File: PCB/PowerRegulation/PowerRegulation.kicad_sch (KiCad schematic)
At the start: 130 parts, among them J1 USB_C_Receptacle_USB2.0_14P, J2 AudioJack3_Ground_Switch, J3 Wii audio in, J4 OLED, SW1 RESET, SW2 BOOT, U1 BQ25883RGER, U10 MCP4651-503E/ST, U11 PAM8403, U2 TPS22918DBVR, U3 STM32F072CBTx, U4 TPS22918DBVR, U5 TPS563200DDCR, U6 TPS563200DDCR, U7 TPS563200DDCR, U8 TPS563200DDCR, U9 TPS563200DDCR

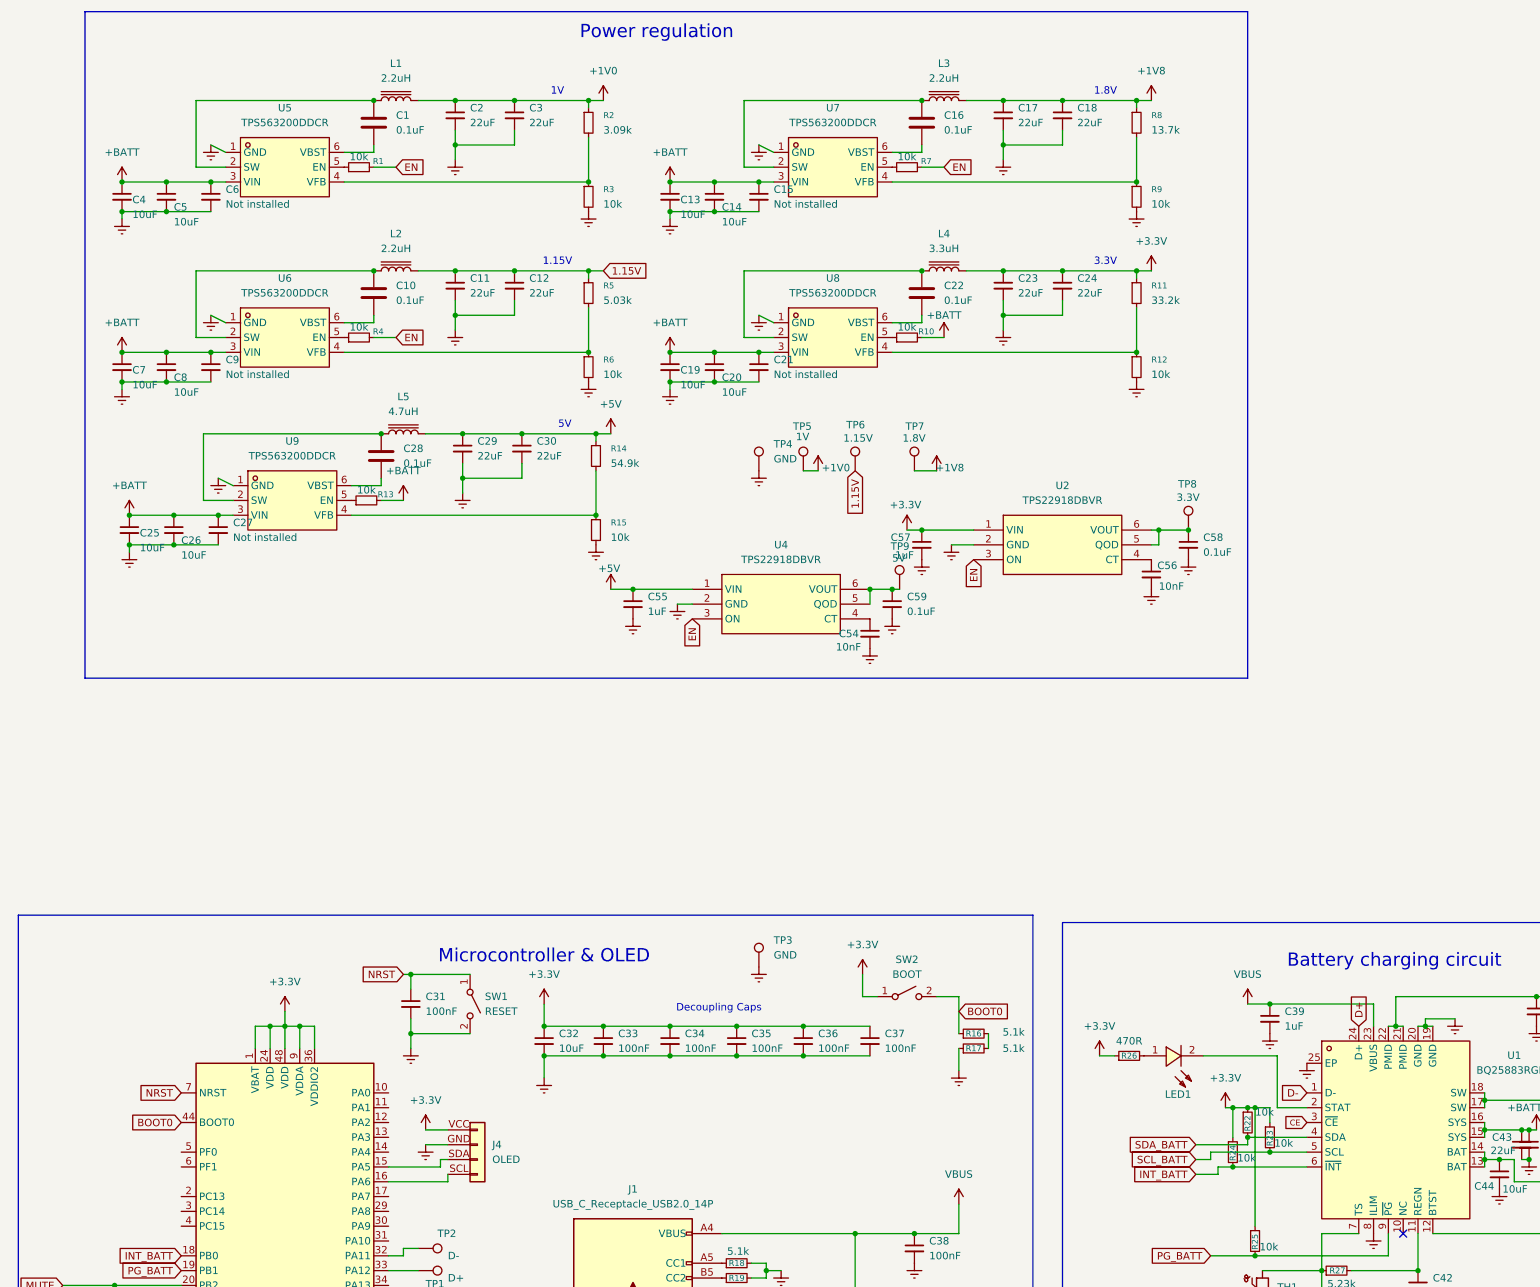
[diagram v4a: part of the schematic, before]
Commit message: Add grounded screws
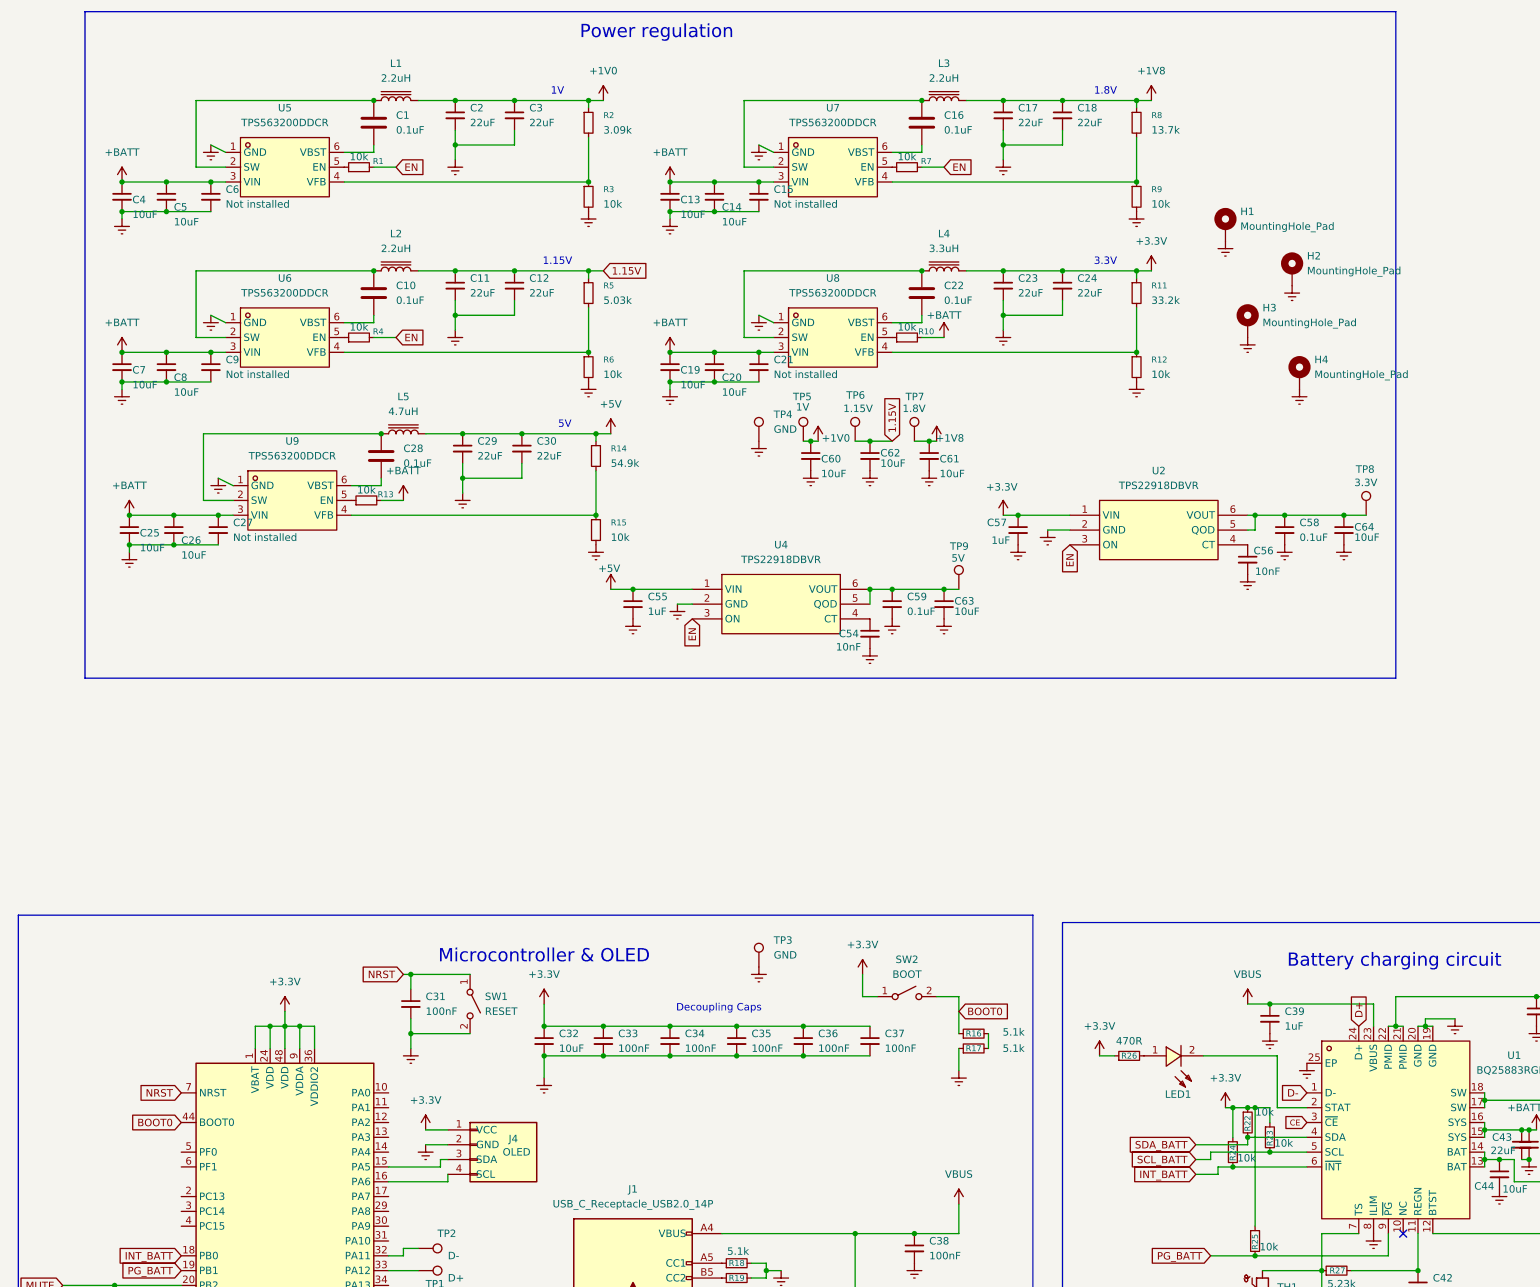
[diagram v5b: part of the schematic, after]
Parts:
- added C60, C61, C62, C63, C64: 10uF, EasyEDA:R0805, symbol Device:C_Small
- added H1, H2, H3, H4: MountingHole_Pad, MountingHole:MountingHole_3.2mm_M3_Pad_Via, symbol Mechanical:MountingHole_Pad
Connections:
- net +1V0: now also C60.1
- net +1V8: now also C61.1
- net +3.3V: now also J4.1 (VCC); no longer J4.VCC (Pin_1)
- net 1.15V: now also C62.1
- net GNDREF: now also J4.2 (GND), C60.2, C61.2, C62.2, C63.2, C64.2, H1.1, H2.1, H3.1, H4.1; no longer J4.GND (Pin_2)
- net at C58.1, TP8.1, U2.5 (QOD)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: now also C64.1
- net at U3.16 (PA6): now also J4.4 (SCL); no longer J4.SCL (Pin_4)
- net at U3.15 (PA5): now also J4.3 (SDA); no longer J4.SDA (Pin_3)
- net at C59.1, TP9.1, U4.5 (QOD)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: now also C63.1
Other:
- moved on the sheet: C56, C57, C58, TP4, TP5, TP6, TP7, TP8, TP9, U2

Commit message: make logo, route some stuff
THIS IS BEFORE THE BATT+ ON In2.Cu
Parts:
- removed J1: USB_C_Receptacle_USB2.0_14P, EasyEDA:USB-C-SMD_TYPE-C-16PIN-2MD-073, symbol Connector:USB_C_Receptacle_USB2.0_14P
- added J1: USB_C_Receptacle_USB2.0_16P, Connector_USB:USB_C_Receptacle_Palconn_UTC16-G, symbol Connector:USB_C_Receptacle_USB2.0_16P
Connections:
- net CE: now also U3.46 (PB9)
- net D+: now also J1.A6 (D+), J1.B6 (D+)
- net D-: now also J1.A7 (D-), J1.B7 (D-)
- net GNDREF: now also J1.A1 (GND), J1.A12 (GND), J1.B1 (GND), J1.B12 (GND), J1.SH (SHIELD)
- net VBUS: now also J1.A4 (VBUS), J1.A9 (VBUS), J1.B4 (VBUS), J1.B9 (VBUS)
- net Debug+: now reaches TP1.1, U3.33 (PA12)
- net at R18.1: now also J1.A5 (CC1)
- net Debug-: now reaches TP2.1, U3.32 (PA11)
- net at R19.1: now also J1.B5 (CC2)
- no-connect marks 3 -> 28
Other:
- moved on the sheet: TP1, TP2

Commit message: route the board
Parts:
- removed J2: AudioJack3_Ground_Switch, symbol Connector_Audio:AudioJack3_Ground_Switch
- added TP12, TP13: TestPoint, TestPoint:TestPoint_Pad_D1.0mm, symbol Connector:TestPoint
- added TP14: L+, TestPoint:TestPoint_Pad_D2.5mm, symbol Connector:TestPoint
- added TP15: R+, TestPoint:TestPoint_Pad_D2.5mm, symbol Connector:TestPoint
- added TP16: GND, TestPoint:TestPoint_Pad_D2.5mm, symbol Connector:TestPoint
- added TP17: L-, TestPoint:TestPoint_Pad_D2.5mm, symbol Connector:TestPoint
- added TP18: R-, TestPoint:TestPoint_Pad_D2.5mm, symbol Connector:TestPoint
- added TP19: S, TestPoint:TestPoint_Pad_D2.0mm, symbol Connector:TestPoint
- added TP20: R, TestPoint:TestPoint_Pad_D2.0mm, symbol Connector:TestPoint
- added TP21: RN, TestPoint:TestPoint_Pad_D2.0mm, symbol Connector:TestPoint
- added TP22: T, TestPoint:TestPoint_Pad_D2.0mm, symbol Connector:TestPoint
- added TP23: TN, TestPoint:TestPoint_Pad_D2.0mm, symbol Connector:TestPoint
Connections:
- net +3.3V: now also TP12.1
- net +5V: now also TP13.1
- net AUDIOL: now also TP23.1
- net AUDIOR: now also TP21.1
- net GNDA: now also TP16.1, TP19.1
- net SPEAKER_L+: now also TP14.1
- net SPEAKER_L-: now also TP17.1
- net SPEAKER_R+: now also TP15.1
- net SPEAKER_R-: now also TP18.1
- net at U10.6 (P1W): now also TP20.1
- net at U10.9 (P0W): now also TP22.1
- no-connect marks 28 -> 27

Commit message: Generate BOM and placement files for JLCPCB
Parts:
- C1, C10, C16, C22, C28, C51: LCSC Part (none) -> C1590
- C11, C12, C17, C18, C2, C23, C24, C29, C3, C30, C43, C53: LCSC Part (none) -> C5672
- C13, C14, C19, C20, C25, C26, C31, C32, C33, C34, C35, C36, C37, C38, C4, C40, C44, C5, C60, C61, C62, C63, C64, C7, C8: LCSC Part (none) -> C1713
- C39, C45, C46, C48, C52: LCSC Part (none) -> C1592
- C41: LCSC Part (none) -> C1622
- C42: LCSC Part (none) -> C1779
- C49, C50: LCSC Part (none) -> C1623
- C54, C56: LCSC Part (none) -> C1846
- C55, C57, C58, C59: LCSC Part (none) -> C1848
- D1: LCSC Part (none) -> C5158049
- FB1: LCSC Part (none) -> C1017
- L1, L2, L3: LCSC Part (none) -> C237985
- L4: LCSC Part (none) -> C189931
- L5: LCSC Part (none) -> C216191
- R1, R10, R12, R13, R15, R22, R23, R24, R25, R3, R31, R32, R4, R6, R7, R9, TH1: LCSC Part (none) -> C1489
- R11: LCSC Part (none) -> C37252
- R14: LCSC Part (none) -> C23077
- R16, R17, R18, R19: LCSC Part (none) -> C23186
- R2: LCSC Part (none) -> C4211
- R20, R21: LCSC Part (none) -> C17506
- R26: LCSC Part (none) -> C436531
- R27: LCSC Part (none) -> C23068
- R28: LCSC Part (none) -> C48533691
- R29, R30: LCSC Part (none) -> C17673
- R5: LCSC Part (none) -> C166926
- R8: LCSC Part (none) -> C22793
- U3: LCSC Part (none) -> C81720
